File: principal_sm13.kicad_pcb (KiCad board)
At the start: 2 copper layers, 138.6 x 86.2 mm, 94 parts, among them J1 Conn_01x03, J2 Conn_01x03, J3 Conn_01x03, J4 Conn_01x03, J5 Conn_01x03, J6 Conn_01x03, J7 Conn_01x03, J8 Conn_01x03, P12 CONN_10X2, P14 SPI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

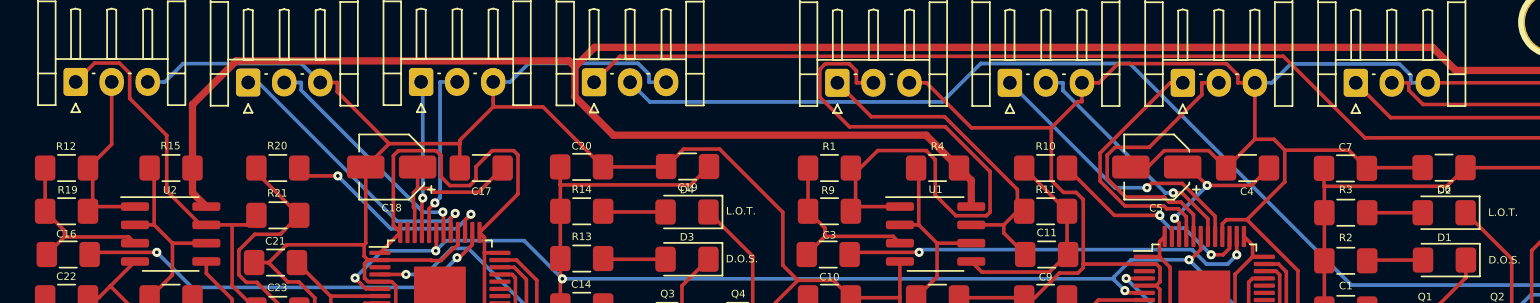
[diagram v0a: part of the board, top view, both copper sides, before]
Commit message: ajustada el area contra los reles
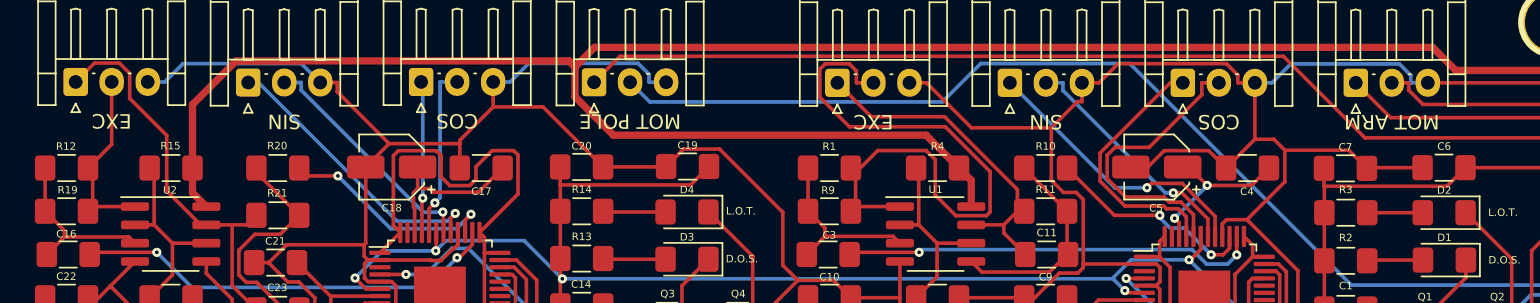
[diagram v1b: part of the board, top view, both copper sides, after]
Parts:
- J1, J4: value Conn_01x03 -> COS
- J2, J5: value Conn_01x03 -> SIN
- J3, J6: value Conn_01x03 -> EXC
- J7: value Conn_01x03 -> MOT ARM
- J8: value Conn_01x03 -> MOT POLE
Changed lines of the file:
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@@
       (effects (font (size 0.52 0.52) (thickness 0.12)))
     )
-    (fp_text value Conn_01x03 (at 2.5 2.7) (layer F.Fab)
+    (fp_text value "MOT POLE" (at 2.5 2.7 180 unlocked) (layer F.SilkS)
       (effects (font (size 1 1) (thickness 0.15)))
     )
@@
       (effects (font (size 0.52 0.52) (thickness 0.12)))
     )
-    (fp_text value Conn_01x03 (at 2.5 2.7) (layer F.Fab)
+    (fp_text value "MOT ARM" (at 2.5 2.7 180 unlocked) (layer F.SilkS)
       (effects (font (size 1 1) (thickness 0.15)))
     )
@@
       (effects (font (size 0.52 0.52) (thickness 0.12)))
     )
-    (fp_text value Conn_01x03 (at 2.5 2.7) (layer F.Fab)
+    (fp_text value EXC (at 2.5 2.7 180 unlocked) (layer F.SilkS)
       (effects (font (size 1 1) (thickness 0.15)))
     )
@@
       (effects (font (size 0.52 0.52) (thickness 0.12)))
     )
-    (fp_text value Conn_01x03 (at 2.5 2.7) (layer F.Fab)
+    (fp_text value SIN (at 2.5 2.7 180 unlocked) (layer F.SilkS)
       (effects (font (size 1 1) (thickness 0.15)))
     )
@@
       (effects (font (size 0.52 0.52) (thickness 0.12)))
     )
-    (fp_text value Conn_01x03 (at 2.5 2.7) (layer F.Fab)
+    (fp_text value COS (at 2.5 2.7 180 unlocked) (layer F.SilkS)
       (effects (font (size 1 1) (thickness 0.15)))
     )
@@
       (effects (font (size 0.52 0.52) (thickness 0.12)))
     )
-    (fp_text value Conn_01x03 (at 2.5 2.7) (layer F.Fab)
+    (fp_text value EXC (at 2.5 2.7 180 unlocked) (layer F.SilkS)
       (effects (font (size 1 1) (thickness 0.15)))
     )
@@
       (effects (font (size 0.52 0.52) (thickness 0.12)))
     )
-    (fp_text value Conn_01x03 (at 2.5 2.7) (layer F.Fab)
+    (fp_text value SIN (at 2.5 2.7 180 unlocked) (layer F.SilkS)
       (effects (font (size 1 1) (thickness 0.15)))
     )
@@
       (effects (font (size 0.52 0.52) (thickness 0.12)))
     )
-    (fp_text value Conn_01x03 (at 2.5 2.7) (layer F.Fab)
+    (fp_text value COS (at 2.5 2.7 180 unlocked) (layer F.SilkS)
       (effects (font (size 1 1) (thickness 0.15)))
     )
@@
     (tags "capacitor handsolder")
     (attr smd)
-    (fp_text reference C19 (at 0 1.45) (layer F.SilkS)
+    (fp_text reference C19 (at 0 -1.47) (layer F.SilkS)
       (effects (font (size 0.52 0.52) (thickness 0.12)))
     )
@@
     (tags "capacitor handsolder")
     (attr smd)
-    (fp_text reference C6 (at 0.01 1.49) (layer F.SilkS)
+    (fp_text reference C6 (at 0.01 -1.48) (layer F.SilkS)
       (effects (font (size 0.52 0.52) (thickness 0.12)))
     )
@@
     (polygon
       (pts
-        (xy 238.655 142.74) (xy 158.685 142.74) (xy 158.689985 139.39) (xy 235.73 139.39)
+        (xy 238.655 142.74) (xy 158.685 142.74) (xy 158.700624 138.92) (xy 235.299376 138.92)
       )
     )

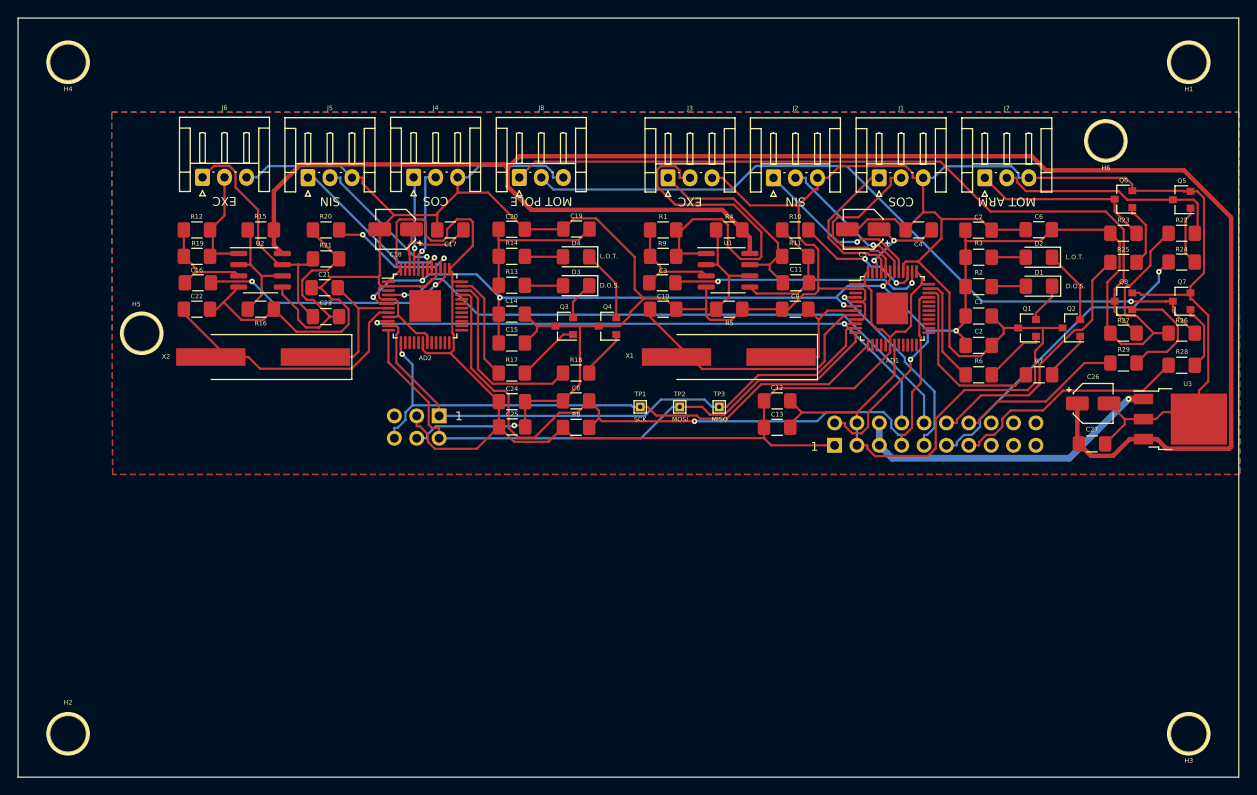
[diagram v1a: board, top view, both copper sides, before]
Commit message: cambiado a conectores MOLEX KK, agregados test points para señales analogicas
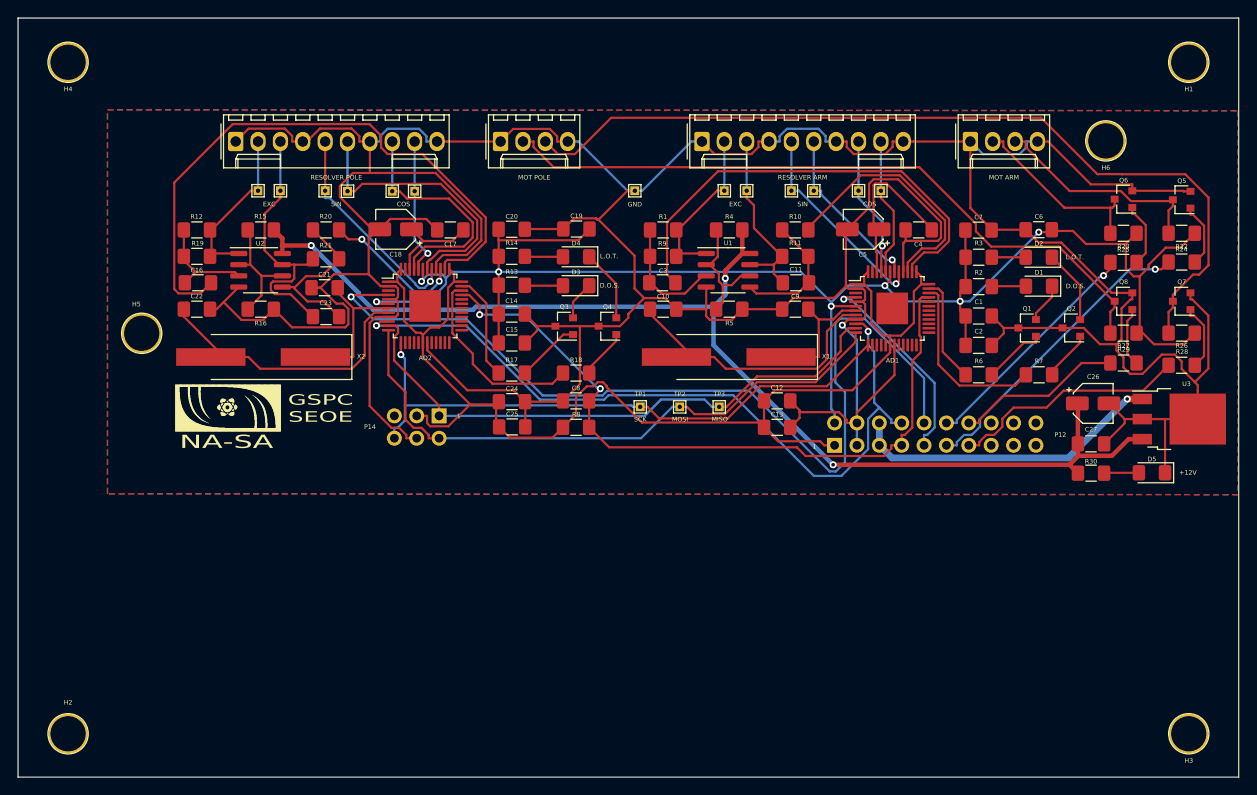
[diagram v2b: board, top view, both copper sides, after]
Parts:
- removed the J3 at (222.1, 108.0)
- removed J5: SIN, Connector_JST:JST_EH_S3B-EH_1x03_P2.50mm_Horizontal
- removed J6: EXC, Connector_JST:JST_EH_S3B-EH_1x03_P2.50mm_Horizontal
- removed J8: MOT POLE, Connector_JST:JST_EH_S3B-EH_1x03_P2.50mm_Horizontal
- added D5: LED, LED_SMD:LED_1206_3216Metric_Pad1.42x1.75mm_HandSolder, F.Cu at (277.1, 141.5)
- added LOGO: , SM13:logo_nasa, F.Cu at (166.2, 131.5)
- added R30: 560, Resistor_SMD:R_1206_3216Metric_Pad1.42x1.75mm_HandSolder, F.Cu at (270.2, 141.5)
- added TP10: TestPoint, TestPoint:TestPoint_THTPad_1.0x1.0mm_Drill0.5mm, F.Cu at (190.8, 109.5)
- added TP11: TestPoint, TestPoint:TestPoint_THTPad_1.0x1.0mm_Drill0.5mm, F.Cu at (193.4, 109.5)
- added TP12: TestPoint, TestPoint:TestPoint_THTPad_1.0x1.0mm_Drill0.5mm, F.Cu at (185.7, 109.5)
- added TP13: TestPoint, TestPoint:TestPoint_THTPad_1.0x1.0mm_Drill0.5mm, F.Cu at (183.2, 109.5)
- added TP14: TestPoint, TestPoint:TestPoint_THTPad_1.0x1.0mm_Drill0.5mm, F.Cu at (175.6, 109.5)
- added TP15: TestPoint, TestPoint:TestPoint_THTPad_1.0x1.0mm_Drill0.5mm, F.Cu at (178.1, 109.5)
- added TP16: GND, TestPoint:TestPoint_THTPad_1.0x1.0mm_Drill0.5mm, F.Cu at (218.4, 109.5)
- added TP4: TestPoint, TestPoint:TestPoint_THTPad_1.0x1.0mm_Drill0.5mm, F.Cu at (243.8, 109.5)
- added TP5: TestPoint, TestPoint:TestPoint_THTPad_1.0x1.0mm_Drill0.5mm, F.Cu at (246.3, 109.5)
- added TP6: TestPoint, TestPoint:TestPoint_THTPad_1.0x1.0mm_Drill0.5mm, F.Cu at (238.7, 109.5)
- added TP7: TestPoint, TestPoint:TestPoint_THTPad_1.0x1.0mm_Drill0.5mm, F.Cu at (236.1, 109.5)
- added TP8: TestPoint, TestPoint:TestPoint_THTPad_1.0x1.0mm_Drill0.5mm, F.Cu at (228.5, 109.5)
- added TP9: TestPoint, TestPoint:TestPoint_THTPad_1.0x1.0mm_Drill0.5mm, F.Cu at (231.1, 109.5)
- J1: value COS -> RESOLVER ARM; footprint Connector_JST:JST_EH_S3B-EH_1x03_P2.50mm_Horizontal -> Connector_Molex:Molex_KK-254_AE-6410-10A_1x10_P2.54mm_Vertical
- J2: value SIN -> RESOLVER POLE; footprint Connector_JST:JST_EH_S3B-EH_1x03_P2.50mm_Horizontal -> Connector_Molex:Molex_KK-254_AE-6410-10A_1x10_P2.54mm_Vertical
- J3: renamed from J7; footprint Connector_JST:JST_EH_S3B-EH_1x03_P2.50mm_Horizontal -> Connector_Molex:Molex_KK-254_AE-6410-04A_1x04_P2.54mm_Vertical
- J4: value COS -> MOT POLE; footprint Connector_JST:JST_EH_S3B-EH_1x03_P2.50mm_Horizontal -> Connector_Molex:Molex_KK-254_AE-6410-04A_1x04_P2.54mm_Vertical
- moved J2 61.2 mm to (173.0, 103.9)
- moved J1 20.5 mm to (226.0, 103.9)
- moved J4 10.7 mm to (203.1, 103.9)
- moved J3 4.44 mm to (256.5, 103.9)
- moved U3 0.13 mm to (280.2, 135.4)
- moved C27 0.11 mm to (270.2, 138.2)
- turned R22 to 180 degrees
- turned R23 to 180 degrees
- turned R26 to 180 degrees
- turned R27 to 180 degrees
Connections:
- J1 pad 1: /RDC ARM/COS -> GND
- J1 pad 2: /RDC ARM/COSLO -> Net-(C3-Pad1)
- J1 pad 3: GND -> Net-(C11-Pad1)
- J2 pad 1: /RDC ARM/SIN -> GND
- J2 pad 2: /RDC ARM/SINLO -> Net-(C16-Pad1)
- J2 pad 3: GND -> Net-(C23-Pad1)
- J3 pad 1: Net-(J7-Pad1) -> GND
- J3 pad 2: Net-(J7-Pad2) -> Net-(J3-Pad2)
- J3 pad 3: GND -> Net-(J3-Pad3)
- J4 pad 1: /RDC POLE/COS -> GND
- J4 pad 2: /RDC POLE/COSLO -> Net-(J4-Pad2)
- J4 pad 3: GND -> Net-(J4-Pad3)
- Q5 pad 3: Net-(J7-Pad2) -> Net-(J3-Pad3)
- Q6 pad 3: Net-(J7-Pad1) -> Net-(J3-Pad2)
- Q7 pad 3: Net-(J8-Pad2) -> Net-(J4-Pad3)
- Q8 pad 3: Net-(J8-Pad1) -> Net-(J4-Pad2)
- R22 pad 2: Net-(J7-Pad2) -> Net-(J3-Pad3)
- R23 pad 2: Net-(J7-Pad1) -> Net-(J3-Pad2)
- R26 pad 2: Net-(J8-Pad2) -> Net-(J4-Pad3)
- R27 pad 2: Net-(J8-Pad1) -> Net-(J4-Pad2)
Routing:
- net Net-(J4-Pad3): track 0.00 -> 99.0 mm
- net Net-(J8-Pad1): track 85.8 -> 0.00 mm
- net Net-(J8-Pad2): track 84.4 -> 0.00 mm, vias 1 -> 0
- net Net-(J4-Pad2): track 0.00 -> 79.6 mm
- net +12V: track 204.7 -> 133.5 mm, vias 0 -> 3
- net GND: track 464.5 -> 531.1 mm
- net /RDC POLE/EXC: track 29.7 -> 69.4 mm, vias 2 -> 0
- net /GPIO/GPIO3: track 70.2 -> 103.9 mm
- net Net-(J7-Pad2): track 26.7 -> 0.00 mm
- net Net-(J3-Pad3): track 0.00 -> 25.1 mm
- net Net-(C3-Pad1): track 43.3 -> 19.2 mm
- net /RDC ARM/EXC: track 29.0 -> 52.6 mm, vias 2 -> 0
- net Net-(J3-Pad2): track 0.00 -> 21.0 mm
- net Net-(J7-Pad1): track 20.7 -> 0.00 mm
- net +3V3: track 148.8 -> 132.3 mm
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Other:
- net class 5V removed
- net class Default: via_dia 0.635 -> 0.8; via_drill 0.254 -> 0.4
- net class POWER-IN: via_dia 0.635 -> 0.8; via_drill 0.254 -> 0.4
- net class POWER-OUT: via_dia 0.635 -> 0.8; via_drill 0.254 -> 0.4
- net class Terminal Block: via_dia 0.635 -> 0.8; via_drill 0.254 -> 0.4
- rule via_min_drill: 0.254 -> 0.4
- rule via_min_size: 0.635 -> 0.8
- board text added: "+12V"
- board text added: "COS"
- board text added: "EXC"
- board text added: "GSPC SEOE"
- board text added: "NA-SA"
- board text added: "SIN"

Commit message: eliminado regulador 12v, alimentar CIAA con 12v directamente
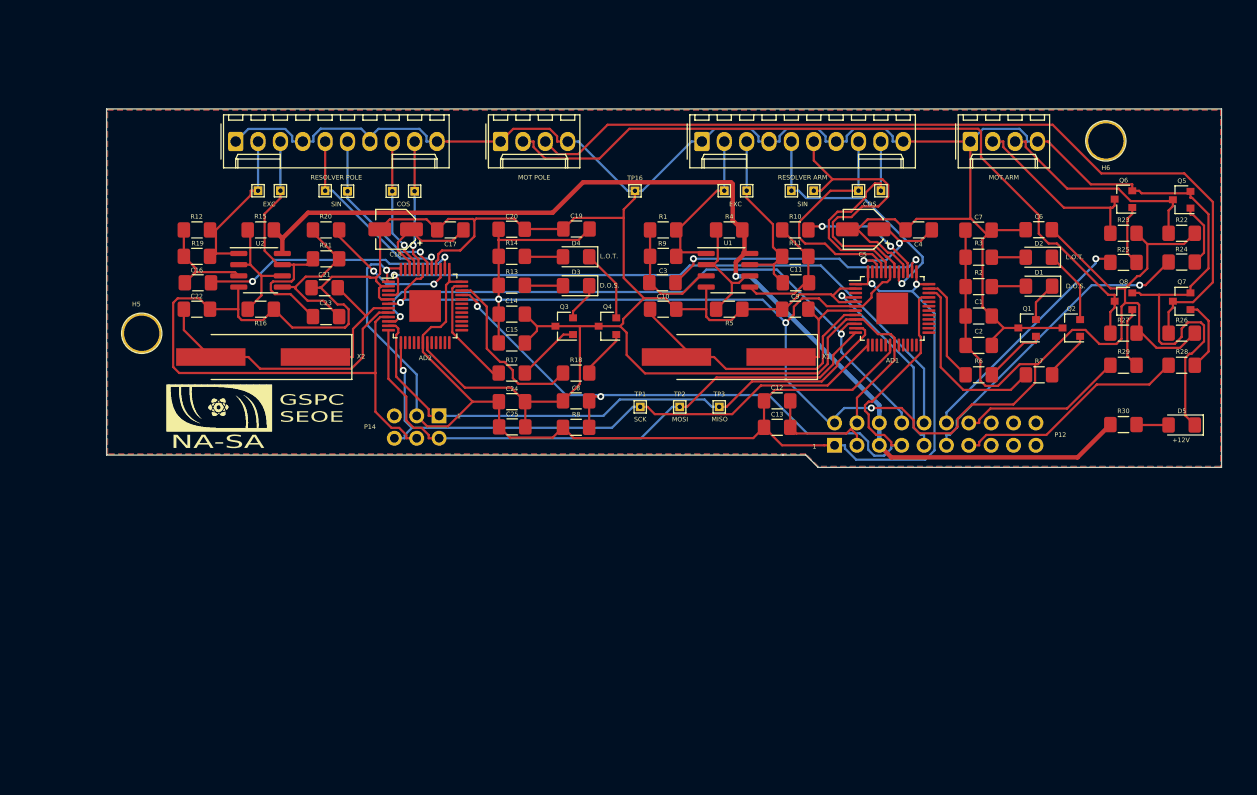
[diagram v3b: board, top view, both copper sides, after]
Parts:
- removed C26: 10µ, Capacitor_SMD:CP_Elec_4x5.4
- removed C27: 0,1µ, Capacitor_SMD:C_1206_3216Metric_Pad1.42x1.75mm_HandSolder
- removed H1, H2, H3, H4: 4mm, 1pin
- removed U3: L7812, Package_TO_SOT_SMD:TO-252-3_TabPin2
- TP10: value TestPoint -> TPCOSPOLE
- TP11: value TestPoint -> TPCOSLOPOLE
- TP12: value TestPoint -> TPSINLOPOLE
- TP13: value TestPoint -> TPSINPOLE
- TP14: value TestPoint -> TPEXCPOLE
- TP15: value TestPoint -> TPEXCLOPOLE
- TP16: value GND -> TPGND
- TP4: value TestPoint -> TPCOSARM
- TP5: value TestPoint -> TPCOSLOARM
- TP6: value TestPoint -> TPSINLOARM
- TP7: value TestPoint -> TPSINARM
- TP8: value TestPoint -> TPEXCARM
- TP9: value TestPoint -> TPEXCLOARM
- moved R30 6.63 mm to (273.8, 136.0)
- moved D5 6.39 mm to (280.5, 136.1)
- moved LOGO 1.00 mm to (165.2, 131.5)
- moved R29 0.25 mm to (273.8, 129.3)
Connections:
- P12 pad 5: +24V -> +12V
- P12 pad 6: +24V -> +12V
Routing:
- net /RDC POLE/EXC: track 69.4 -> 29.5 mm, vias 0 -> 2
- net +24V: track 35.8 -> 0.00 mm, vias 1 -> 0
- net +5V: track 184.8 -> 217.7 mm, vias 7 -> 4
- net +3V3: track 132.3 -> 164.5 mm, vias 0 -> 3
- net /GPIO/GPIO3: track 103.9 -> 75.0 mm
- net /RDC ARM/EXC: track 52.6 -> 31.1 mm, vias 0 -> 2
- net /RDC ARM/~EXC: track 28.9 -> 14.2 mm, vias 0 -> 2
- net /RDC ARM/SINLO: track 19.4 -> 34.0 mm, vias 1 -> 0
- net /RDC POLE/SINLO: track 32.1 -> 19.6 mm, vias 0 -> 1
- net /GPIO/GPIO1: track 86.0 -> 74.3 mm
- net /RDC POLE/COS: track 26.9 -> 15.5 mm, vias 0 -> 1
- net /RDC ARM/COS: track 16.0 -> 27.1 mm, vias 1 -> 0
- net +12V: track 133.5 -> 124.2 mm, vias 3 -> 1
- net /RDC ARM/COSLO: track 15.8 -> 25.1 mm
- net /RDC ARM/SIN: track 23.3 -> 29.1 mm
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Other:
- board size 138.6 x 86.2 mm -> 126.6 x 40.7 mm

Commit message: cambiados capacitores electroliticos por tantalio (unpolarized). Agrandado footprint test pads, generado BOM, 35 vias
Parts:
- C18, C5: footprint Capacitor_SMD:CP_Elec_4x5.4 -> Capacitor_SMD:C_1206_3216Metric_Pad1.42x1.75mm_HandSolder
- TP1, TP10, TP11, TP12, TP13, TP14, TP15, TP16, TP2, TP3, TP4, TP5, TP6, TP7, TP8, TP9: footprint TestPoint:TestPoint_THTPad_1.0x1.0mm_Drill0.5mm -> TestPoint:TestPoint_THTPad_1.5x1.5mm_Drill0.7mm
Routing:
- net GND: track 532.0 -> 504.3 mm
- net +3V3: track 164.5 -> 143.1 mm, vias 3 -> 4
- net +5V: track 217.7 -> 198.8 mm, vias 4 -> 5
- net /GPIO/GPIO1: track 74.3 -> 91.2 mm, vias 2 -> 1
- net Net-(J4-Pad3): track 99.8 -> 84.5 mm, vias 0 -> 1
- net /RDC ARM/SINLO: track 34.0 -> 20.3 mm, vias 0 -> 1
- net /RDC ARM/COS: track 27.1 -> 15.9 mm, vias 0 -> 1
- net /RDC ARM/COSLO: track 25.1 -> 15.2 mm, vias 0 -> 1
- net /RDC POLE/~EXC: track 15.7 -> 23.6 mm, vias 2 -> 0
- net /RDC ARM/SIN: track 29.1 -> 23.2 mm
- net Net-(J4-Pad2): track 85.1 -> 80.6 mm, vias 0 -> 1
- net /GPIO/GPIO0: track 87.3 -> 83.1 mm
- net /RDC ARM/MOSI: track 68.7 -> 72.8 mm, vias 0 -> 1
- net /RDC POLE/SINLO: track 19.6 -> 23.1 mm
- net /RDC POLE/SIN: track 22.3 -> 25.8 mm
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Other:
- board text added: "GND"

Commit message: agrandados pads de test points
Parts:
- TP1, TP10, TP11, TP12, TP13, TP14, TP15, TP16, TP2, TP3, TP4, TP5, TP6, TP7, TP8, TP9: footprint TestPoint:TestPoint_THTPad_1.5x1.5mm_Drill0.7mm -> TestPoint:TestPoint_reducido
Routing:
- net GND: track 504.3 -> 530.7 mm, vias 0 -> 2
- net /RDC ARM/SIN: track 23.2 -> 40.9 mm, vias 1 -> 0
- net Net-(J4-Pad3): track 84.5 -> 101.3 mm, vias 1 -> 0
- net +5V: track 198.8 -> 209.9 mm
- net /RDC ARM/~EXC: track 15.0 -> 25.8 mm, vias 2 -> 0
- net /GPIO/GPIO0: track 83.1 -> 90.1 mm
- net Net-(J4-Pad2): track 80.6 -> 86.1 mm, vias 1 -> 0
- net /RDC POLE/SINLO: track 23.1 -> 19.0 mm
- net /RDC ARM/MISO: track 67.0 -> 71.0 mm
- net Net-(AD2-Pad46): track 16.0 -> 12.0 mm
- net +12V: track 122.8 -> 118.8 mm
- net /GPIO/GPIO3: track 75.9 -> 79.7 mm
- net /GPIO/SPI_SCK: track 71.0 -> 74.5 mm
- net /GPIO/GPIO1: track 91.2 -> 87.9 mm, vias 1 -> 2
- net Net-(AD2-Pad7): track 17.0 -> 20.1 mm
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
